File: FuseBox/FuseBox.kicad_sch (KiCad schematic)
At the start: 38 parts, among them J1 UJ31-CH-G2-SMT-TR, U1 TPS61040DBVR, U2 LT3030EFE_TRPBF

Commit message: Changes
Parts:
- added TP1, TP2: TestPoint, symbol Connector:TestPoint
- R3: value 910k -> 873k3
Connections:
- net +5V: now also TP1.1
- net VBUS: now also TP2.1
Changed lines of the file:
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@@
 	(wire
 		(pts
+			(xy 97.79 161.29) (xy 97.79 162.56)
+		)
+		(stroke
+			(width 0)
+			(type default)
+		)
+	)
+	(wire
+		(pts
 			(xy 163.83 125.73) (xy 163.83 127)
 		)
@@
 	(wire
 		(pts
+			(xy 38.1 161.29) (xy 38.1 162.56)
+		)
+		(stroke
+			(width 0)
+			(type default)
+		)
+	)
+	(wire
+		(pts
 			(xy 138.43 138.43) (xy 142.24 138.43)
 		)
@@
 	)
 	(symbol
+		(lib_id "Connector:TestPoint")
+		(at 97.79 161.29 0)
+		(unit 1)
+		(exclude_from_sim no)
+		(in_bom yes)
+		(on_board yes)
+		(dnp no)
+		(fields_autoplaced yes)
+		(property "Reference" "TP1"
+			(at 100.33 156.7179 0)
+			(effects
+				(font
+					(size 1.27 1.27)
+				)
+				(justify left)
+			)
+		)
+		(property "Value" "TestPoint"
+			(at 100.33 159.2579 0)
+			(effects
+				(font
+					(size 1.27 1.27)
+				)
+				(justify left)
+			)
+		)
+		(property "Footprint" ""
+			(at 102.87 161.29 0)
+			(effects
+				(font
+					(size 1.27 1.27)
+				)
+				(hide yes)
+			)
+		)
+		(property "Datasheet" "~"
+			(at 102.87 161.29 0)
+			(effects
+				(font
+					(size 1.27 1.27)
+				)
+				(hide yes)
+			)
+		)
+		(property "Description" "test point"
+			(at 97.79 161.29 0)
+			(effects
+				(font
+					(size 1.27 1.27)
+				)
+				(hide yes)
+			)
+		)
+		(pin "1"
+		)
+		(instances
+			(project ""
+				(path "/7cec0856-4a31-46c4-b6e3-cba19fcff38c"
+					(reference "TP1")
+					(unit 1)
+				)
+			)
+		)
+	)
+	(symbol
 		(lib_id "power:GND")
 		(at 199.39 71.12 0)
@@
 			)
 		)
-		(property "Value" "910k"
+		(property "Value" "873k3"
 			(at 227.33 53.3399 0)
 			(effects
@@
 					(unit 1)
 				)
+			)
+		)
+	)
+	(symbol
+		(lib_id "Connector:TestPoint")
+		(at 38.1 161.29 0)
+		(unit 1)
+		(exclude_from_sim no)
+		(in_bom yes)
+		(on_board yes)
+		(dnp no)
+		(fields_autoplaced yes)
+		(property "Reference" "TP2"
+			(at 40.64 156.7179 0)
+			(effects
+				(font
+					(size 1.27 1.27)
+				)
+				(justify left)
+			)
+		)
+		(property "Value" "TestPoint"
+			(at 40.64 159.2579 0)
+			(effects
+				(font
+					(size 1.27 1.27)
+				)
+				(justify left)
+			)
+		)
+		(property "Footprint" ""
+			(at 43.18 161.29 0)
+			(effects
+				(font
+					(size 1.27 1.27)
+				)
+				(hide yes)
+			)
+		)
+		(property "Datasheet" "~"
+			(at 43.18 161.29 0)
+			(effects
+				(font
+					(size 1.27 1.27)
+				)
+				(hide yes)
+			)
+		)
+		(property "Description" "test point"
+			(at 38.1 161.29 0)
+			(effects
+				(font
+					(size 1.27 1.27)
+				)
+				(hide yes)
+			)
+		)
+		(pin "1"
+		)
+		(instances
+			(project "FuseBox"
+				(path "/7cec0856-4a31-46c4-b6e3-cba19fcff38c"
+					(reference "TP2")
+					(unit 1)
+				)

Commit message: added models
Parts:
- removed D1: CUS10S40_H3F, Custom:CUS10S40H3F, symbol Custom:CUS10S40_H3F
- removed J1: UJ31-CH-G2-SMT-TR, Custom:UJ31CHG2SMTTR, symbol Custom:UJ31-CH-G2-SMT-TR
- removed U2: LT3030EFE_TRPBF, Custom:LT8302ES8E_TRPBF, symbol Custom:LT3030EFE_TRPBF
- added D1: CUS10S40H3F, Custom:CUS10S40H3F, symbol Custom:CUS10S40H3F
- added J1: UJ31CHG2SMTTR, Custom:UJ31CHG2SMTTR, symbol Custom:UJ31CHG2SMTTR
- added U2: LT3030EFETRPBF, Custom:LT8302ES8ETRPBF, symbol Custom:LT3030EFETRPBF
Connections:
- net +12V4: now also D1.1
- net +1V22: now also U2.10 (ADJ2), U2.7 (OUT2), U2.8 (OUT2)
- net +3V31: now also U2.3 (OUT1), U2.4 (OUT1)
- net +5V: now also U2.11 (*SHDN2), U2.13 (IN2), U2.14 (IN2), U2.17 (IN1), U2.18 (IN1), U2.20 (*SHDN1)
- net GND: now also J1.A1 (GND_1), J1.A12 (GND_2), J1.B1 (GND_3), J1.B12 (GND_4), J1.S1 (GND_5), J1.S2 (GND_6), J1.S3 (GND_7), J1.S4 (GND_8), U2.15 (GND), U2.16 (GND), U2.5 (GND), U2.6 (GND)
- net USB_OTG_FS_DN: now also J1.A7 (DN1), J1.B7 (DN2)
- net USB_OTG_FS_DP: now also J1.A6 (DP1), J1.B6 (DP2)
- net VBUS: now also J1.A4 (V_BUS_1), J1.A9 (V_BUS_2), J1.B4 (VBUS_1), J1.B9 (VBUS_2)
- net at L1.2, U1.1 (SW): now also D1.2
- net at R2.1: now also J1.A5 (CC1)
- net at C8.2: now also U2.2 (BYP1)
- net at C9.2: now also U2.9 (BYP2)
- net at R8.1, R9.2: now also U2.1 (ADJ1)
- net at R6.1: now also U2.12 (PWRGD2)
- net at R1.1: now also J1.B5 (CC2)
- net at R7.1: now also U2.19 (PWRGD1)

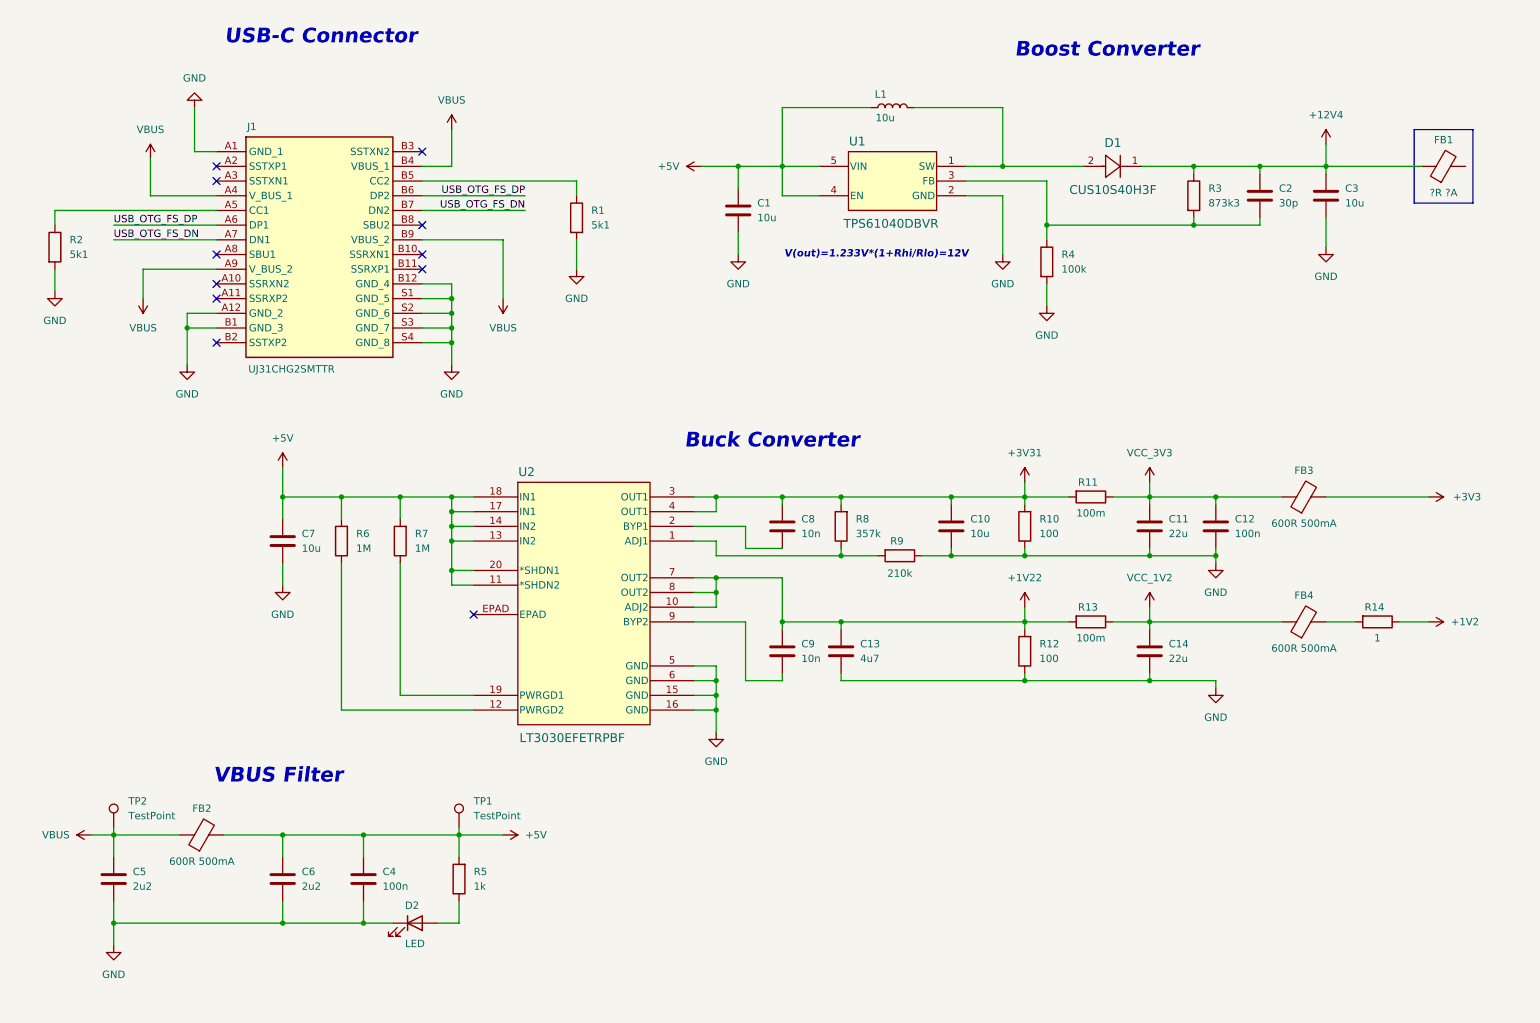
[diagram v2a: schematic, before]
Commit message: Added STM32F4
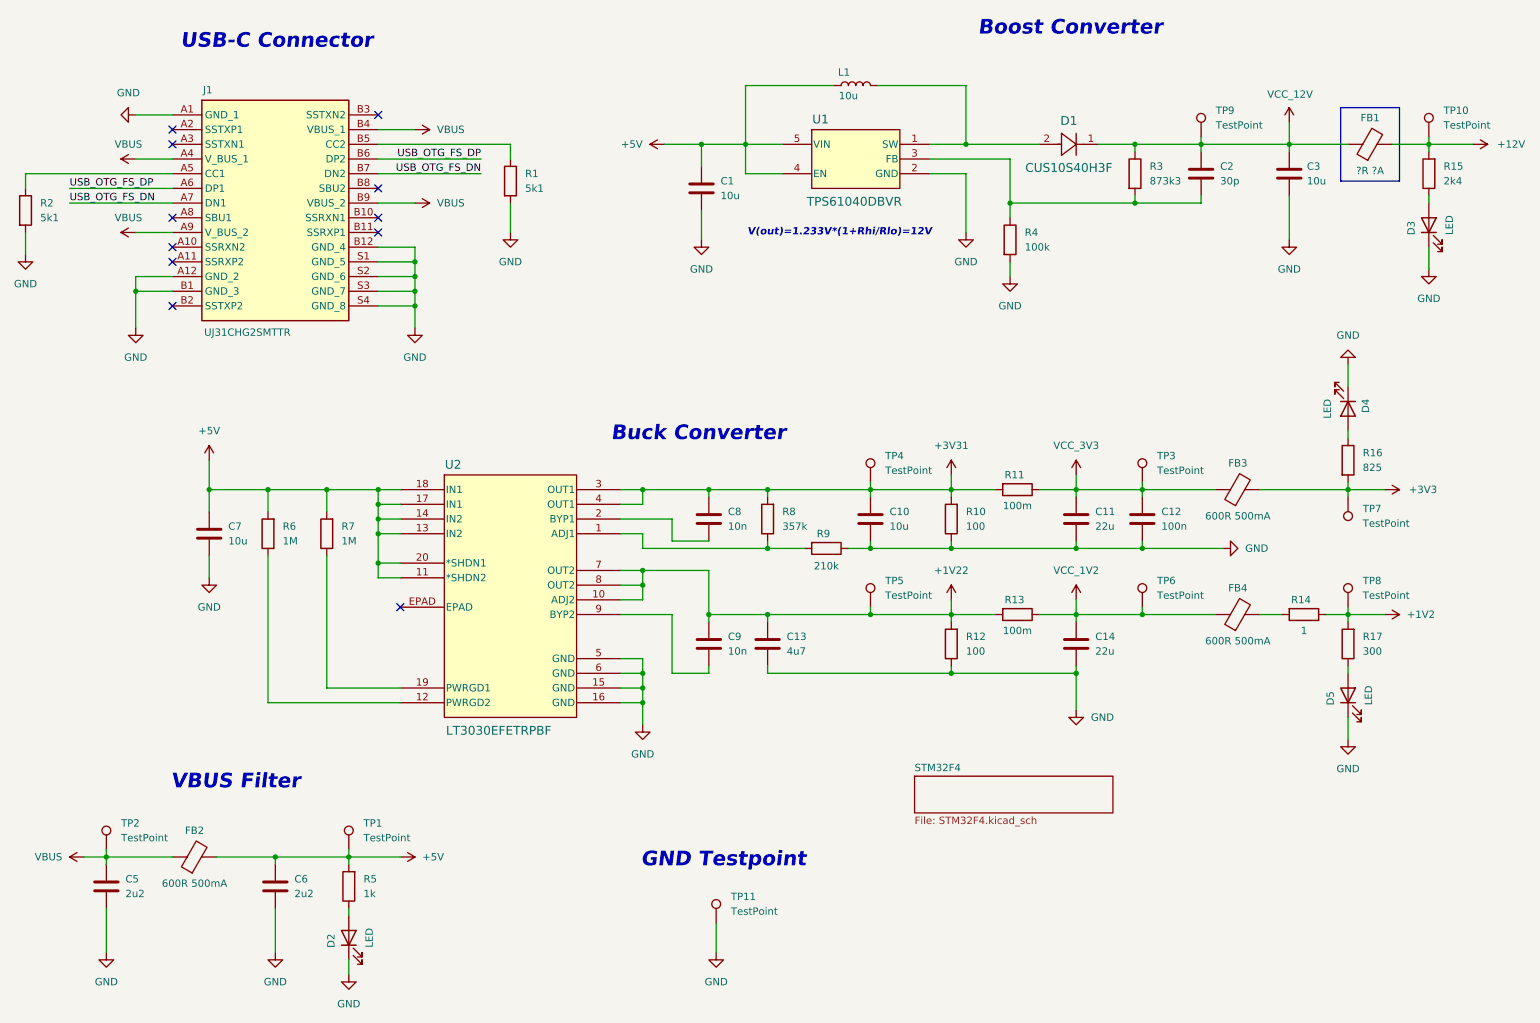
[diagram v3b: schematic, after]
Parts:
- removed C4: 100n, symbol Device:C
- added D3, D4, D5: LED, symbol Device:LED
- added R15: 2k4, symbol Device:R
- added R16: 825, symbol Device:R
- added R17: 300, symbol Device:R
- added TP10, TP11, TP3, TP4, TP5, TP6, TP7, TP8, TP9: TestPoint, symbol Connector:TestPoint
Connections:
- net +1V2: now also R17.2, TP8.1
- net +1V22: now also TP5.1
- net +3V3: now also R16.2, TP7.1
- net +3V31: now also TP4.1
- net GND: now also D3.1 (K), D4.1 (K), D5.1 (K), TP11.1
- net VCC_1V2: now also TP6.1
- net VCC_3V3: now also TP3.1
- net +12V: now reaches FB1.2
- net +12V: now also R15.2, TP10.1
- net +12V4 renamed VCC_12V
- net VCC_12V: now also TP9.1
- new net: D3.2 (A), R15.1
- new net: D5.2 (A), R17.1
- new net: D4.2 (A), R16.1
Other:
- added sheet STM32F4 (STM32F4.kicad_sch)
- note added: "GND Testpoint"
- moved on the sheet: C1, C10, C11, C12, C13, C14, C2, C3, C5, C6, C7, C8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
